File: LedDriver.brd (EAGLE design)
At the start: 100 x 80 mm, 18 parts, among them IC1 CAT4101, IC2 CAT4101, X1 MKDSN1,5/3-5,08, X2 MKDSN1,5/4-5,08

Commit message: vwersion 1.0
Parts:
- C1: value (none) -> 10u; device rcl:E3,5-8 -> rcl:C1210
- C2, C3: value (none) -> 100n
- D1, D2, D3: value (none) -> 5.6V; device diode:DO35Z10 -> diode:SOD80C
- R1, R2, R3: value (none) -> 5k
- R4, R5: value (none) -> 2.7k
- moved X1 69.5 mm to (41.9, 11.4), turned to 270 degrees
- moved Q3 66.9 mm to (16.8, 12.5)
- moved C1 56.4 mm to (11.9, 16.2)
- moved Q2 55.1 mm to (16.6, 24.4)
- moved Q1 36.6 mm to (12.2, 20.1), turned to 270 degrees
- moved R1 30.8 mm to (12.2, 22.8), turned to 0 degrees
- moved D1 29.8 mm to (15.0, 25.0), flipped to the bottom, turned to 180 degrees
- moved X2 28.8 mm to (4.16, 14.2)
- moved IC1 27.1 mm to (28.4, 20.0)
- moved IC2 26.9 mm to (28.3, 8.00)
- moved R5 26.9 mm to (16.2, 7.25)
- moved C3 26.7 mm to (17.8, 9.06)
- moved C2 26.6 mm to (17.8, 20.9)
- moved R4 26.5 mm to (16.2, 19.2)
- moved D3 25.9 mm to (11.9, 9.65)
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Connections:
- net GND: now also C1.2, X2.1; no longer C1.-, X2.4
- net N$3: now also X2.3; no longer X2.2
- net N$5: now also X2.2; no longer X2.3
- net VCC: now also C1.1, X2.4; no longer C1.+, X2.1
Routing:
- net GND: track 0.00 -> 175.6 mm, vias 0 -> 33
- net VCC: track 0.00 -> 56.5 mm, vias 0 -> 1
- net N$15: track 0.00 -> 24.7 mm, vias 0 -> 1
- net N$9: track 0.00 -> 23.9 mm, vias 0 -> 2
- net N$14: track 0.00 -> 23.2 mm, vias 0 -> 1
- net N$3: track 0.00 -> 17.4 mm
- net N$5: track 0.00 -> 13.4 mm
- net N$11: track 0.00 -> 4.13 mm
- net N$1: track 0.00 -> 4.12 mm
- net N$10: track 0.00 -> 4.10 mm
- net N$6: track 0.00 -> 3.99 mm
- net N$4: track 0.00 -> 3.80 mm
- net N$7: track 0.00 -> 2.84 mm
- net N$8: track 0.00 -> 2.62 mm
- added copper zone on layer 1, net GND
- added copper zone on layer 16, net GND
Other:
- board size 100 x 80 mm -> 46 x 28 mm

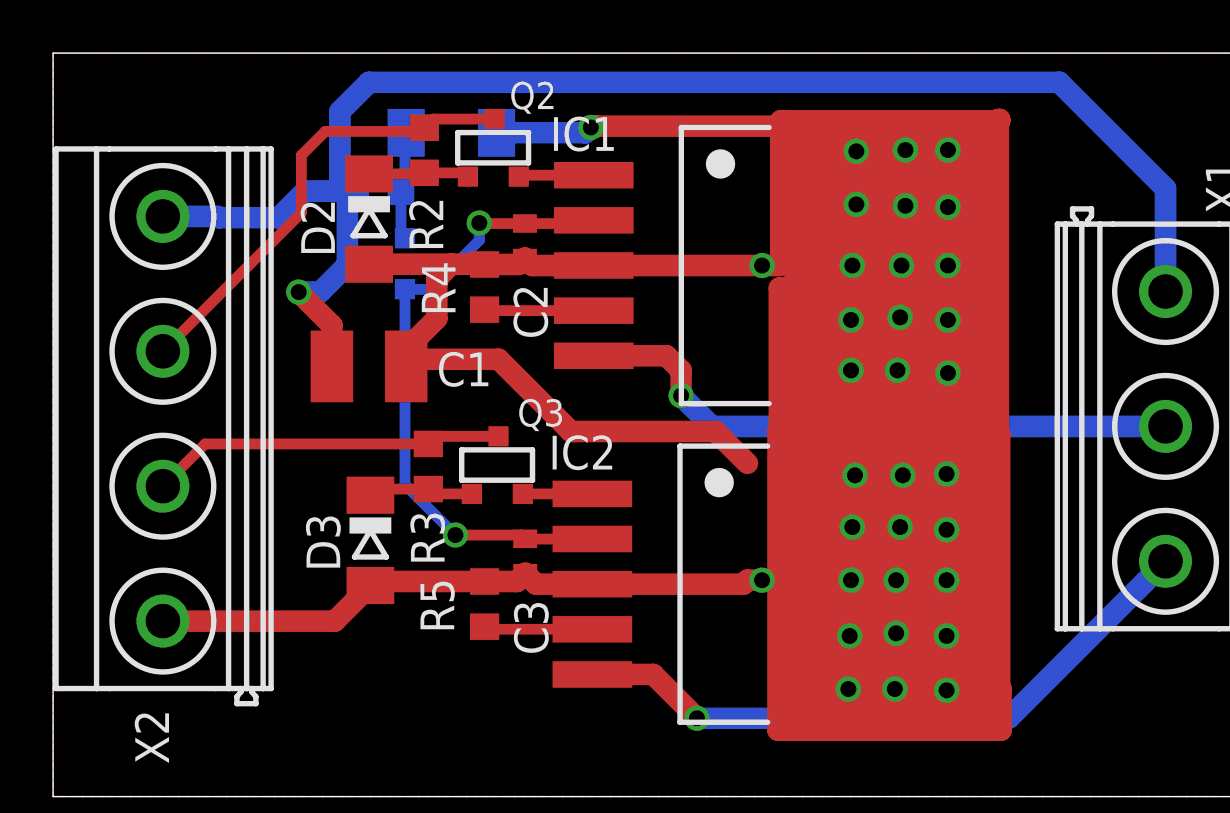
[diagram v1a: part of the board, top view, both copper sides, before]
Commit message: added pull up resistors for enable pin
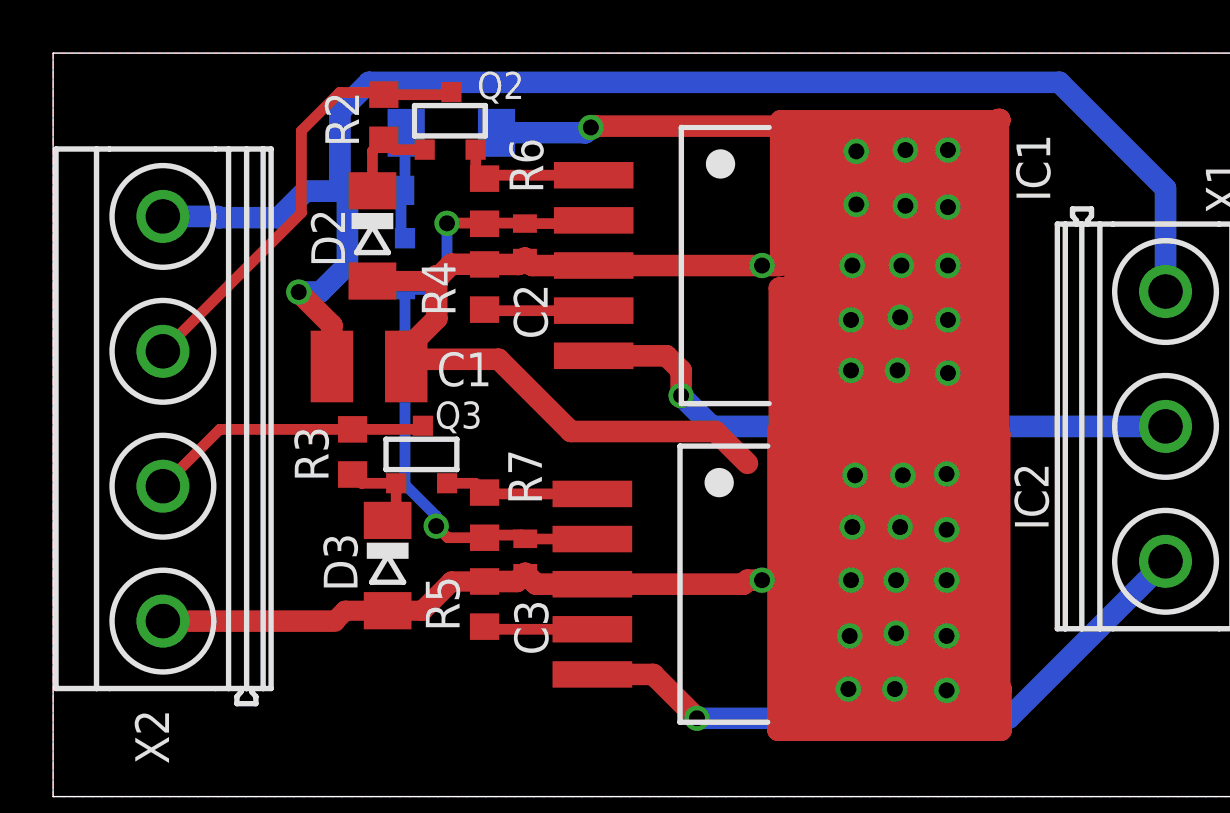
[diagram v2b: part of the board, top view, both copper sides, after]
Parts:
- added R6, R7: 100k, rcl:R0603
- moved R3 2.90 mm to (11.3, 13.0)
- moved Q3 2.88 mm to (13.9, 12.9)
- moved R2 1.97 mm to (12.5, 25.6)
- moved Q2 1.92 mm to (15.0, 25.5)
- moved D3 1.15 mm to (12.6, 8.70)
- moved D2 0.65 mm to (12.0, 21.1)
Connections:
- net N$7: now also R6.1
- net N$8: now also R7.1
- net N$9: now also R6.2, R7.2
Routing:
- net N$8: track 2.62 -> 5.64 mm
- net N$5: track 13.4 -> 10.7 mm
- net N$7: track 2.84 -> 5.40 mm
- net N$9: track 23.9 -> 25.2 mm
- net N$6: track 3.99 -> 3.31 mm
- net GND: track 175.6 -> 174.9 mm
- net N$3: track 17.4 -> 16.8 mm
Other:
- board text added: "LED Driver v1.1"

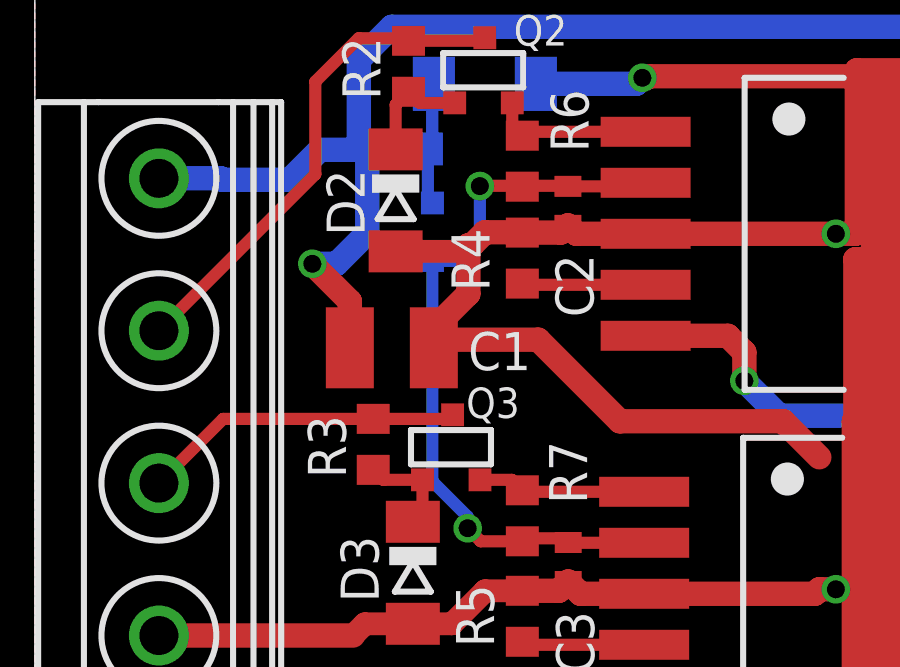
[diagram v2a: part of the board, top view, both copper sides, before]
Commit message: added reverse polarity protection diode
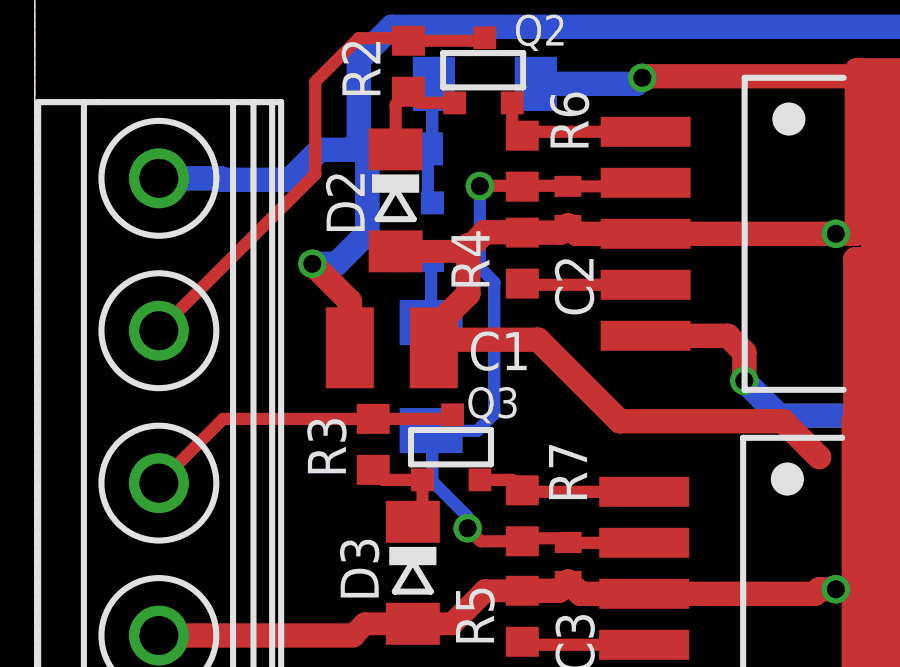
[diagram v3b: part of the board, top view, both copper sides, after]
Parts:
- added D4: CGRM4001-G, diode:SOD-123_MINI-SMA
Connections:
- new net N$2: D4.A, Q1.2
- net N$9: now also D4.C; no longer Q1.2
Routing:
- net N$2: track 0.00 -> 2.09 mm
- net N$9: track 25.2 -> 26.0 mm
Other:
- board text added: "+"
- board text added: "-(1)"
- board text added: "-(2)"
- board text added: "12V"
- board text added: "GND"
- board text added: "PWM1"
- board text added: "PWM2"
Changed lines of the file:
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@@
 <wire x1="0" y1="28" x2="0" y2="0" width="0" layer="20"/>
 <text x="36.2712" y="3.5814" size="1.778" layer="26" font="vector" rot="MR90">LED Driver v1.1</text>
+<text x="2.0574" y="24.1808" size="1.27" layer="26" font="vector" rot="MR270">12V</text>
+<text x="2.1082" y="8.3312" size="1.27" layer="26" font="vector" rot="MR270">GND</text>
+<text x="2.1082" y="19.6088" size="1.27" layer="26" font="vector" rot="MR270">PWM1</text>
+<text x="2.1336" y="14.224" size="1.27" layer="26" font="vector" rot="MR270">PWM2</text>
+<text x="45.1612" y="19.7866" size="1.27" layer="26" font="vector" rot="MR270">+</text>
+<text x="45.0088" y="15.3416" size="1.27" layer="26" font="vector" rot="MR270">-(1)</text>
+<text x="45.2374" y="10.5664" size="1.27" layer="26" font="vector" rot="MR270">-(2)</text>
 </plain>
 <attributes>
@@
 </element>
 <element name="Q1" library="transistors" package="SOT-23" value="" x="12.15" y="20.05" smashed="yes" rot="MR270">
-<attribute name="NAME" x="12.658" y="18.018" size="1.016" layer="22" ratio="12" rot="MR270"/>
+<attribute name="NAME" x="14.9948" y="20.8882" size="1.016" layer="22" ratio="12" rot="MR270"/>
 <attribute name="VALUE" x="14.563" y="18.018" size="1.016" layer="22" ratio="12" rot="MR270"/>
 </element>
@@
 <attribute name="NAME" x="17.139" y="13.0892" size="1.27" layer="25" rot="R270"/>
 <attribute name="VALUE" x="14.345" y="11.235" size="1.27" layer="27" rot="R270"/>
+</element>
+<element name="D4" library="diode" package="SOD-123_MINI-SMA" value="CGRM4001-G" x="13.208" y="15.24" smashed="yes" rot="MR90">
+<attribute name="NAME" x="14.732" y="13.9192" size="1.27" layer="26" rot="MR90"/>
+<attribute name="VALUE" x="10.795" y="12.192" size="1.27" layer="28" rot="MR90"/>
 </element>
 </elements>
@@
 </signal>
 <signal name="N$9">
-<contactref element="Q1" pad="2"/>
 <contactref element="IC1" pad="2"/>
 <contactref element="C2" pad="1"/>
@@
 <wire x1="17.77" y1="21.58" x2="20.24" y2="21.58" width="0.4064" layer="1"/>
 <wire x1="20.24" y1="21.58" x2="20.36" y2="21.7" width="0.4064" layer="1"/>
-<wire x1="14.2" y1="19.1" x2="13.2616" y2="19.1" width="0.4064" layer="16"/>
-<wire x1="13.2616" y1="19.1" x2="13.2514" y2="19.1102" width="0.4064" layer="16"/>
 <wire x1="20.31" y1="9.7" x2="17.79" y2="9.7" width="0.4064" layer="1"/>
 <wire x1="17.79" y1="9.7" x2="17.78" y2="9.71" width="0.4064" layer="1"/>
-<wire x1="13.2514" y1="19.1102" x2="13.2514" y2="11.7486" width="0.4064" layer="16"/>
 <wire x1="17.64" y1="9.85" x2="17.78" y2="9.71" width="0.4064" layer="1"/>
 <contactref element="R7" pad="2"/>
@@
 <wire x1="14.8436" y1="21.6" x2="14.8336" y2="21.59" width="0.4064" layer="1"/>
 <via x="14.8336" y="21.59" extent="1-16" drill="0.6"/>
-<wire x1="14.8336" y1="21.59" x2="14.8336" y2="19.7336" width="0.4064" layer="16"/>
-<wire x1="14.8336" y1="19.7336" x2="14.2" y2="19.1" width="0.4064" layer="16"/>
+<wire x1="14.8336" y1="21.59" x2="14.8336" y2="18.8722" width="0.4064" layer="16"/>
 <wire x1="16.2492" y1="21.571" x2="16.5318" y2="21.571" width="0.4064" layer="1"/>
 <wire x1="16.5318" y1="21.571" x2="16.5608" y2="21.6" width="0.4064" layer="1"/>
+<contactref element="D4" pad="C"/>
+<wire x1="13.2514" y1="11.7486" x2="13.2514" y2="13.3966" width="0.4064" layer="16"/>
+<wire x1="13.2514" y1="13.3966" x2="13.208" y2="13.44" width="0.4064" layer="16"/>
+<wire x1="14.8336" y1="18.8722" x2="15.3162" y2="18.3896" width="0.4064" layer="16"/>
+<wire x1="15.3162" y1="18.3896" x2="15.3162" y2="13.9954" width="0.4064" layer="16"/>
+<wire x1="15.3162" y1="13.9954" x2="14.7574" y2="13.4366" width="0.4064" layer="16"/>
+<wire x1="14.7574" y1="13.4366" x2="13.2114" y2="13.4366" width="0.4064" layer="16"/>
+<wire x1="13.2114" y1="13.4366" x2="13.208" y2="13.44" width="0.4064" layer="16"/>
 </signal>
 <signal name="N$11">
@@
 <wire x1="35.9839" y1="2.95" x2="41.895" y2="8.8611" width="0.8128" layer="16"/>
 </signal>
+<signal name="N$2">
+<contactref element="Q1" pad="2"/>
+<contactref element="D4" pad="A"/>
+<wire x1="13.208" y1="17.04" x2="13.208" y2="19.0668" width="0.4064" layer="16"/>
+<wire x1="13.208" y1="19.0668" x2="13.2514" y2="19.1102" width="0.4064" layer="16"/>
+</signal>
 </signals>
